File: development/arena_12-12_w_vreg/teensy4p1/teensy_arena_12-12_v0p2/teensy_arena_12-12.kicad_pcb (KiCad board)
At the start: 4 copper layers, 226.6 x 226.6 mm, 123 parts, among them J1 Barrel_Jack, J2 Conn_01x04, J3 Conn_01x04, P1 CONN15, P10 CONN15, P11 CONN15, P12 CONN15, P2 CONN15, P3 CONN15, P4 CONN15, P5 CONN15, P6 CONN15, P7 CONN15, P8 CONN15, P9 CONN15, Q2 MOSFET_NCHAN, SW1 SW_SPDT, U1 TXB0108PW, U10 TPS564201DDC, U11 TPS564201DDC, U12 TPS564201DDC, U13 TPS564201DDC, U14 TPS564201DDC, U15 TPS564201DDC, U16 TPS564201DDC, U17 TPS564201DDC, U18 Teensy4.1, U2 TXB0108PW, U3 TXB0108PW, U4 TXB0108PW, U5 TXB0108PW, U6 TPS564201DDC, U7 TPS564201DDC, U8 TPS564201DDC, U9 TPS564201DDC

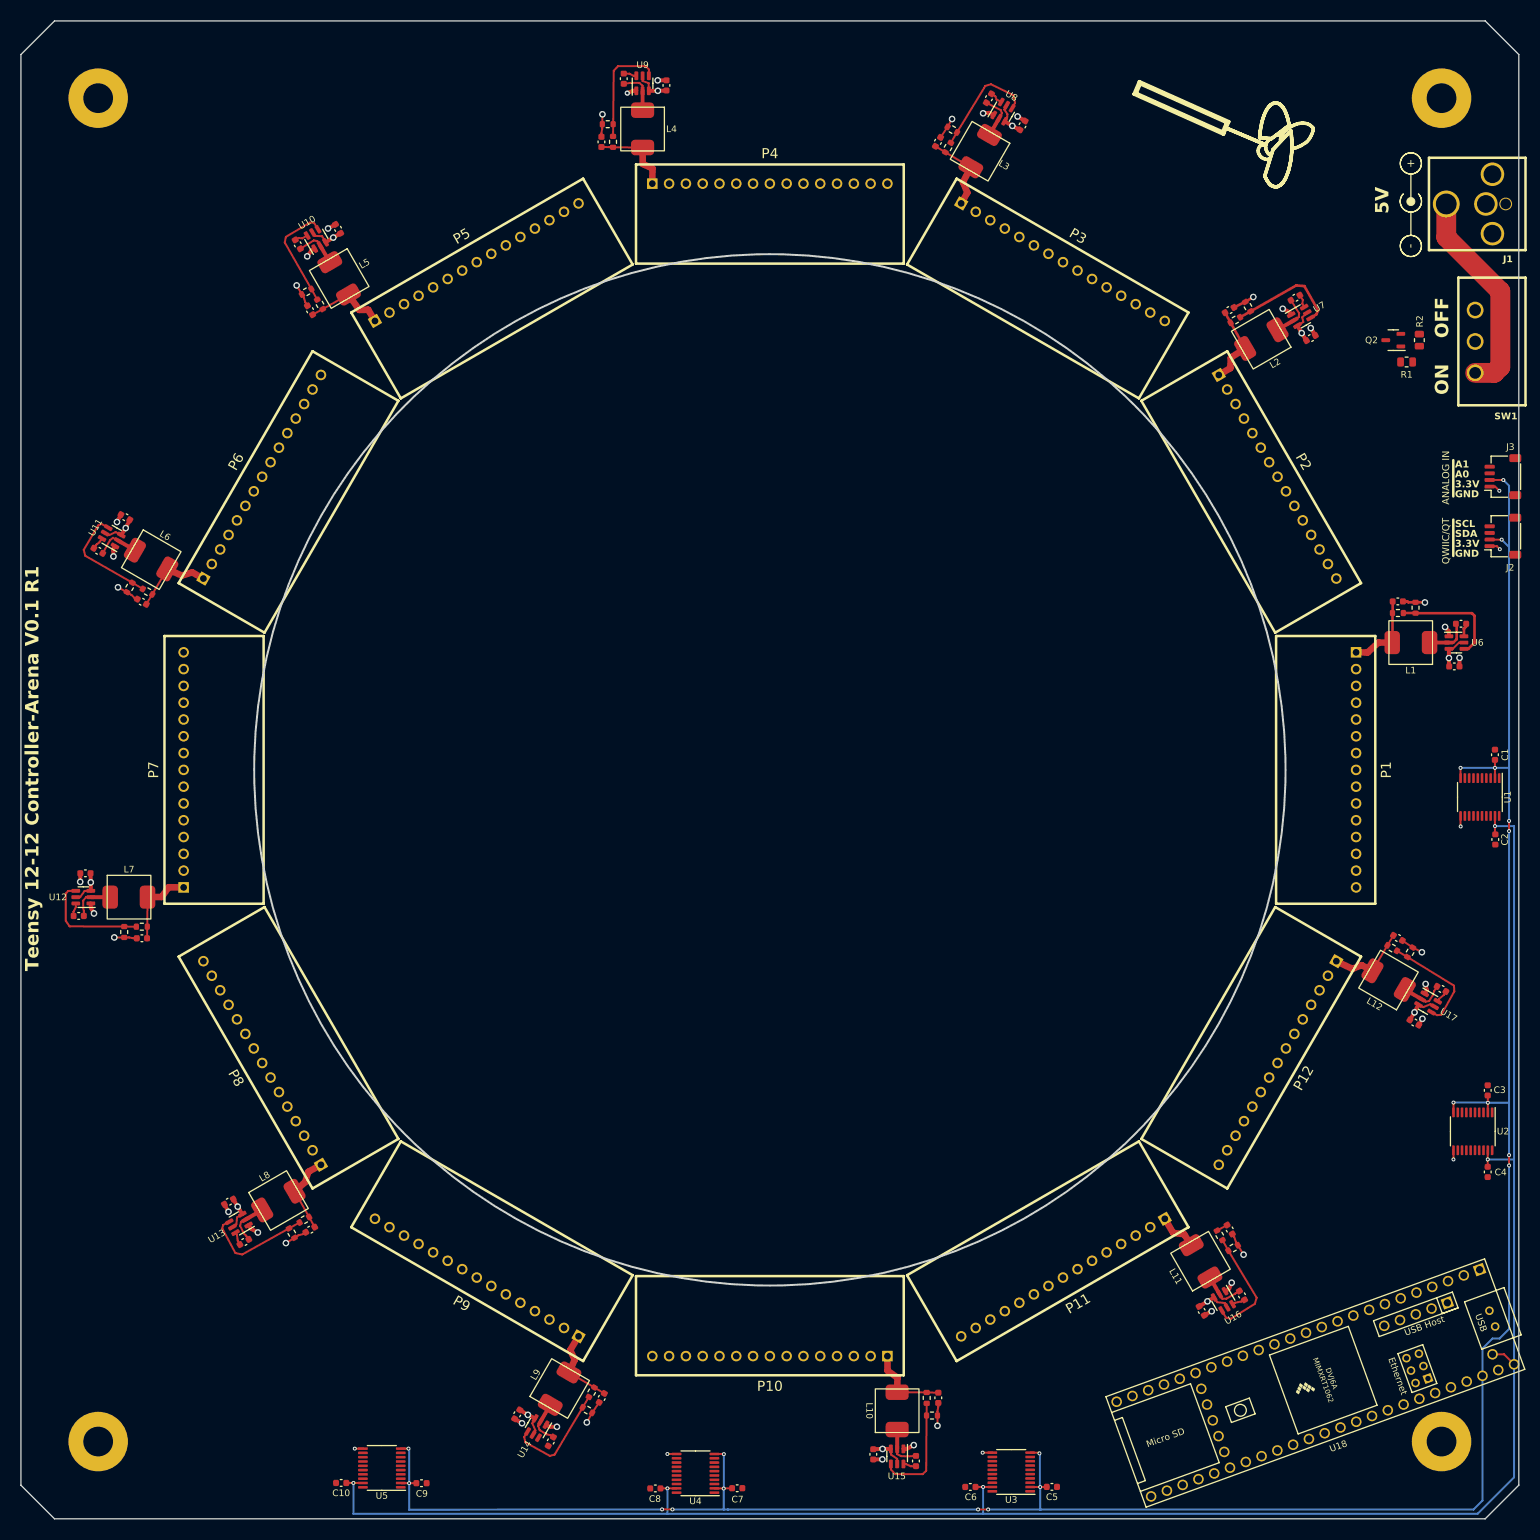
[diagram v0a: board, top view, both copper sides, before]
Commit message: More work on routing.
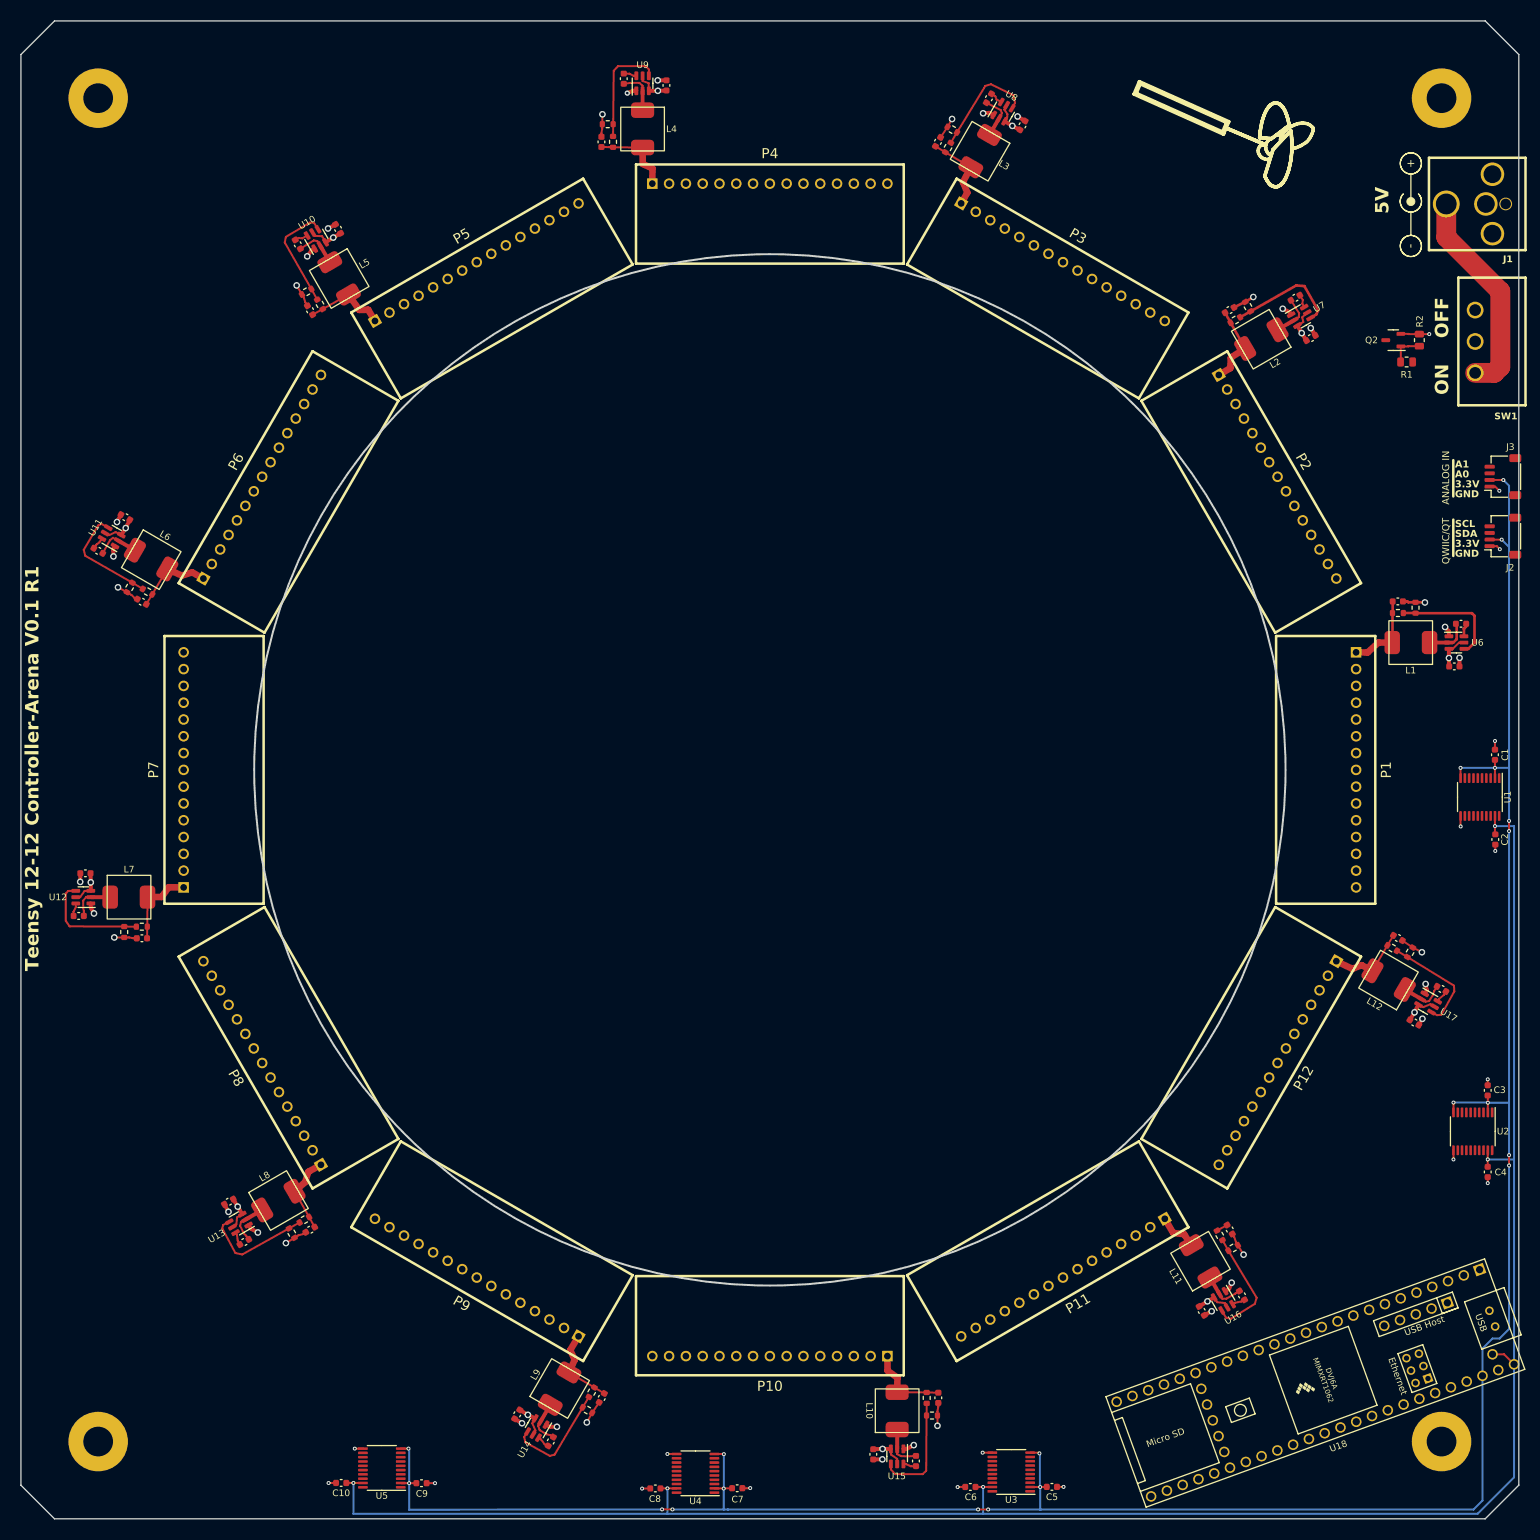
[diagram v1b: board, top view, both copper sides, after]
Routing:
- net GND: track 87.3 -> 102.7 mm, vias 43 -> 54
- net Net-(Q2-G): track 0.00 -> 5.19 mm
- net Net-(U14-VBST): track 0.00 -> 1.98 mm

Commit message: Worked on routing for ni and teensy vreg arenas.
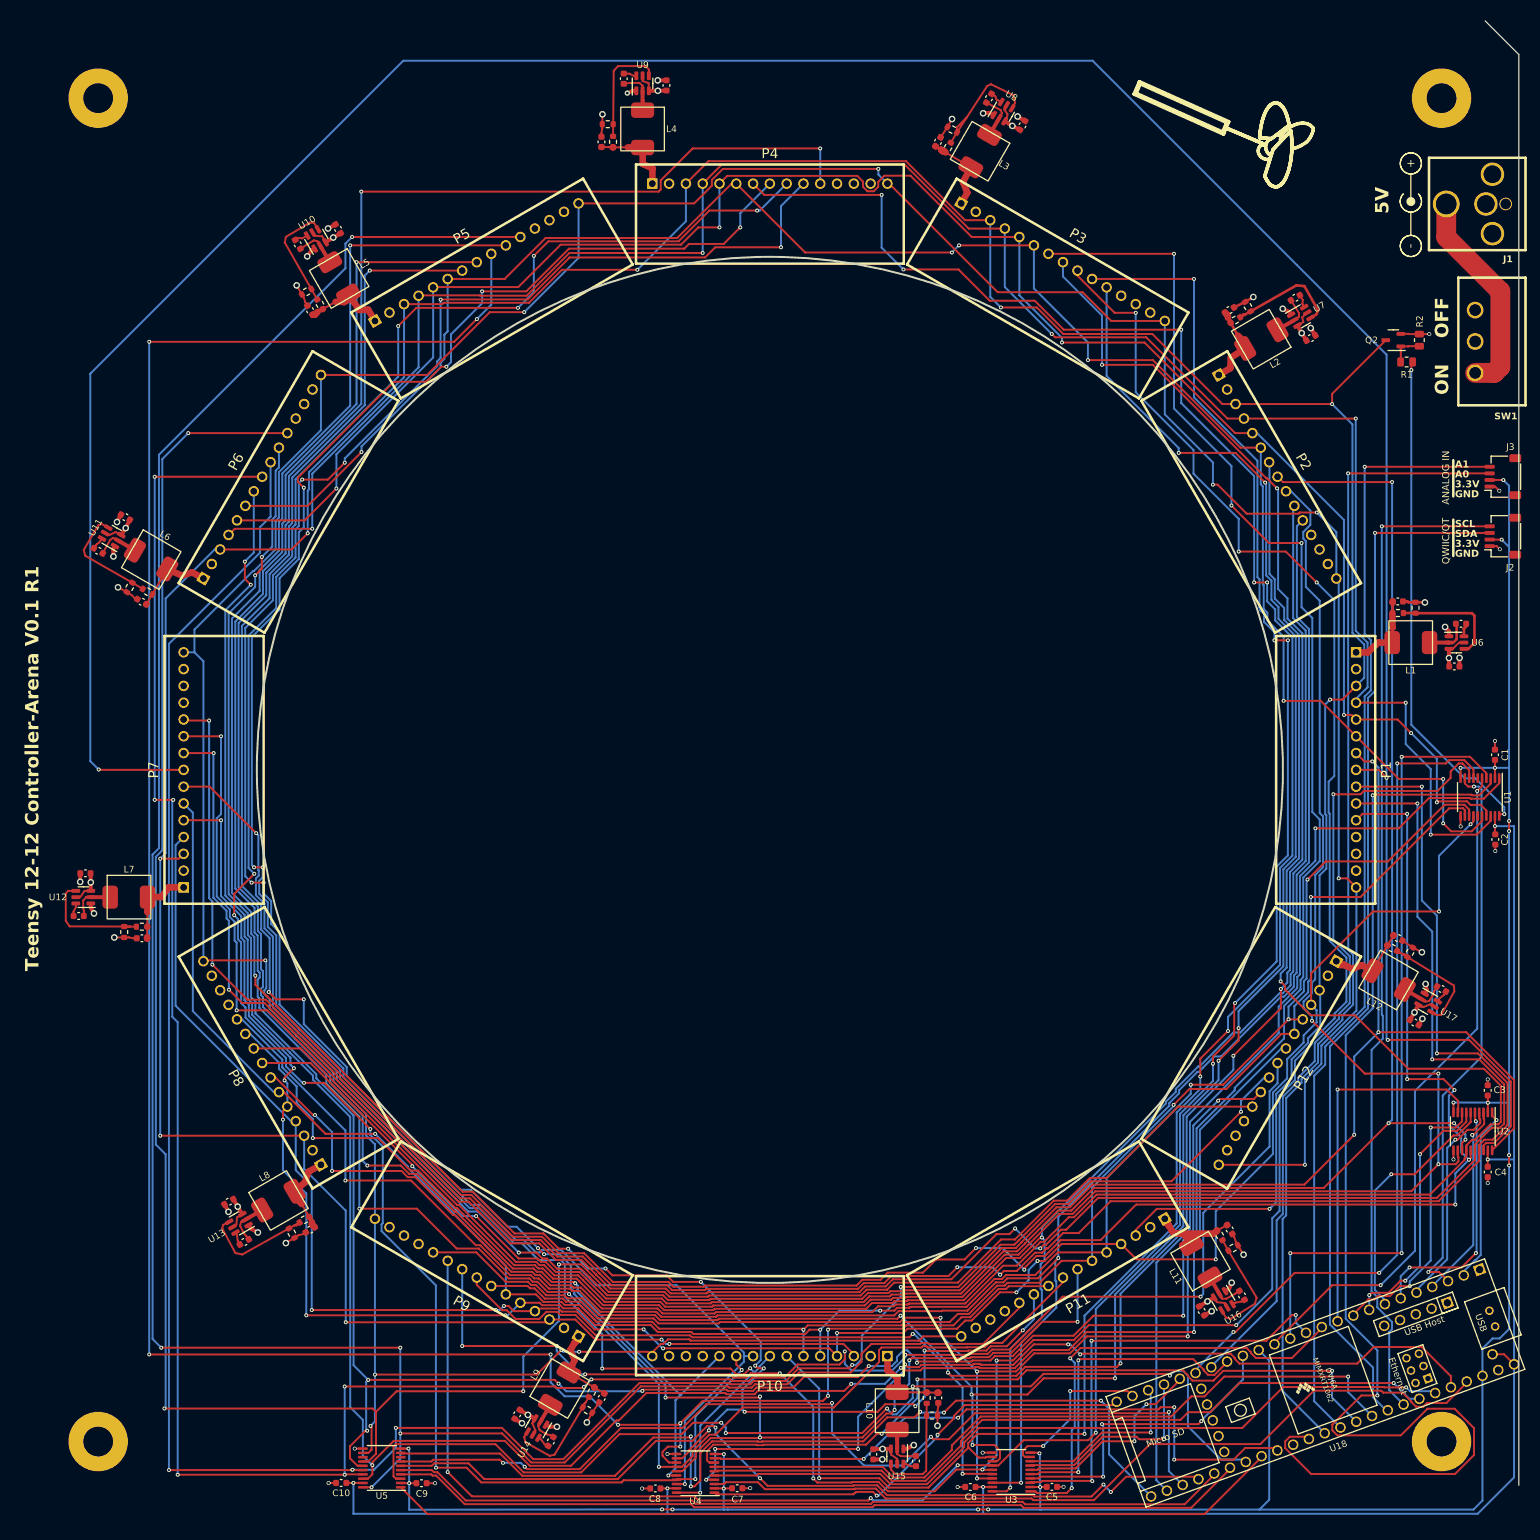
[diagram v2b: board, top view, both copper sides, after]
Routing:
- net /Panel Headers/RESET: track 0.00 -> 624.9 mm, vias 0 -> 11
- net /Level Shifters/PAN5V.EXT_INT: track 0.00 -> 603.1 mm, vias 0 -> 11
- net /Level Shifters/PAN5V.CS_01: track 0.00 -> 450.2 mm, vias 0 -> 3
- net /Level Shifters/PAN5V.CS_26: track 0.00 -> 391.9 mm, vias 0 -> 11
- net /Level Shifters/PAN5V.CS_22: track 0.00 -> 382.1 mm, vias 0 -> 9
- net /Level Shifters/PAN5V.CS_24: track 0.00 -> 373.8 mm, vias 0 -> 5
- net /Level Shifters/PAN5V.CS_29: track 0.00 -> 370.1 mm, vias 0 -> 4
- net /Level Shifters/PAN5V.CS_27: track 0.00 -> 361.2 mm, vias 0 -> 6
- net /Level Shifters/PAN5V.CS_12: track 0.00 -> 355.6 mm, vias 0 -> 11
- net /Level Shifters/PAN5V.CS_25: track 0.00 -> 347.8 mm, vias 0 -> 6
- net /Level Shifters/PAN5V.CS_13: track 0.00 -> 345.4 mm, vias 0 -> 9
- net /Level Shifters/PAN5V.CS_05: track 0.00 -> 344.7 mm, vias 0 -> 3
- net /Level Shifters/PAN5V.CS_28: track 0.00 -> 341.4 mm, vias 0 -> 10
- net /Level Shifters/PAN5V.CS_03: track 0.00 -> 339.9 mm, vias 0 -> 6
- net /Level Shifters/PAN5V.CS_10: track 0.00 -> 336.7 mm, vias 0 -> 7
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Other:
- board size 226.6 x 226.6 mm -> 190.9 x 221.5 mm

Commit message: Worked on routing of ni 12-12 arena with vreg.
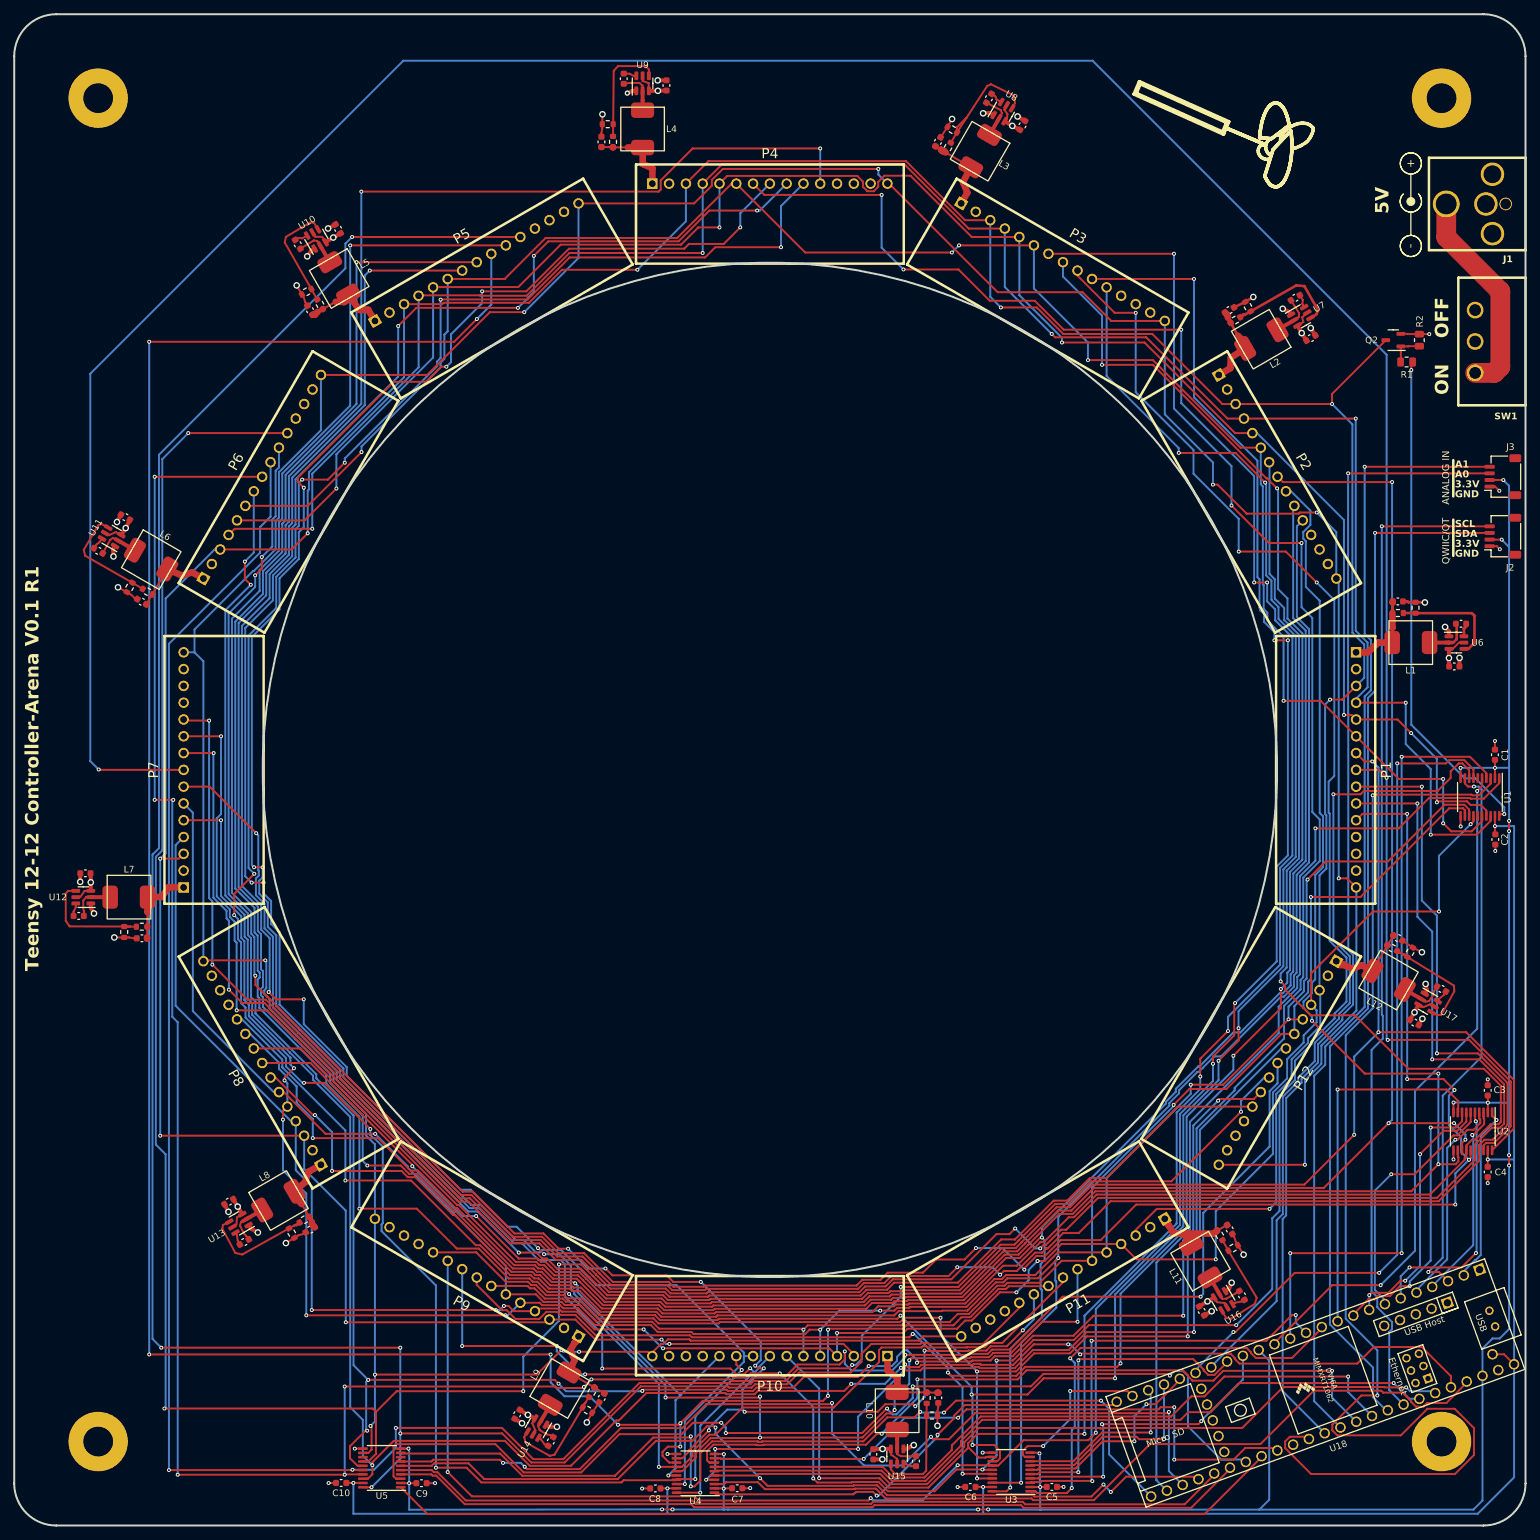
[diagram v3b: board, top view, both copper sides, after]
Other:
- board size 190.9 x 221.5 mm -> 228.6 x 228.6 mm
